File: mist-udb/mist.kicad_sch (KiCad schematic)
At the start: 26 parts, among them J1 78171-0004, J2 Conn_01x05, Q3 MMUN2133LT1G, U3 XC6206PxxxMR-Regulator_Linear, U4 CR2013-MI2120, U5 STM32G474RETx, U6 SN74AHCT1G125DBVR

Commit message: Updated UDB files
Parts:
- added H1, H2, H3, H4, H5, H6: MountingHole_Pad, MountingHole:MountingHole_3.2mm_M3_DIN965_Pad, symbol Mechanical:MountingHole_Pad
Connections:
- net GND: now also H1.1, H2.1, H3.1, H4.1, H5.1, H6.1

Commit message: Updated standoff sizes
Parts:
- H1, H2, H3, H4, H5, H6: footprint MountingHole:MountingHole_3.2mm_M3_DIN965_Pad -> MountingHole:MountingHole_2.2mm_M2_DIN965_Pad
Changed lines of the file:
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@@
 			)
 		)
-		(property "Footprint" "MountingHole:MountingHole_3.2mm_M3_DIN965_Pad"
+		(property "Footprint" "MountingHole:MountingHole_2.2mm_M2_DIN965_Pad"
 			(at 342.9 135.89 0)
 			(effects
@@
 			)
 		)
-		(property "Footprint" "MountingHole:MountingHole_3.2mm_M3_DIN965_Pad"
+		(property "Footprint" "MountingHole:MountingHole_2.2mm_M2_DIN965_Pad"
 			(at 340.36 111.76 0)
 			(effects
@@
 			)
 		)
-		(property "Footprint" "MountingHole:MountingHole_3.2mm_M3_DIN965_Pad"
+		(property "Footprint" "MountingHole:MountingHole_2.2mm_M2_DIN965_Pad"
 			(at 340.36 121.92 0)
 			(effects
@@
 			)
 		)
-		(property "Footprint" "MountingHole:MountingHole_3.2mm_M3_DIN965_Pad"
+		(property "Footprint" "MountingHole:MountingHole_2.2mm_M2_DIN965_Pad"
 			(at 340.36 132.08 0)
 			(effects
@@
 			)
 		)
-		(property "Footprint" "MountingHole:MountingHole_3.2mm_M3_DIN965_Pad"
+		(property "Footprint" "MountingHole:MountingHole_2.2mm_M2_DIN965_Pad"
 			(at 342.9 115.57 0)
 			(effects
@@
 			)
 		)
-		(property "Footprint" "MountingHole:MountingHole_3.2mm_M3_DIN965_Pad"
+		(property "Footprint" "MountingHole:MountingHole_2.2mm_M2_DIN965_Pad"
 			(at 342.9 125.73 0)
 			(effects

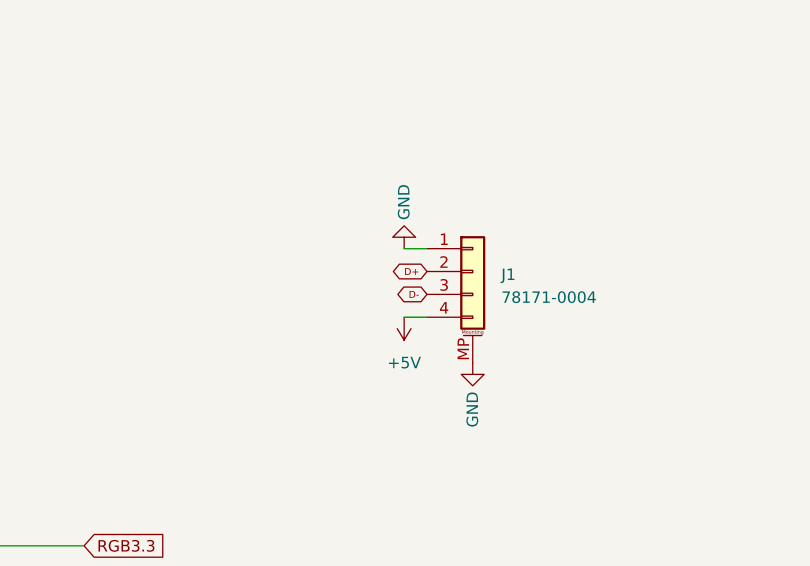
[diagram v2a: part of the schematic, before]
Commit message: Fixed UDB pinout, had it backwards
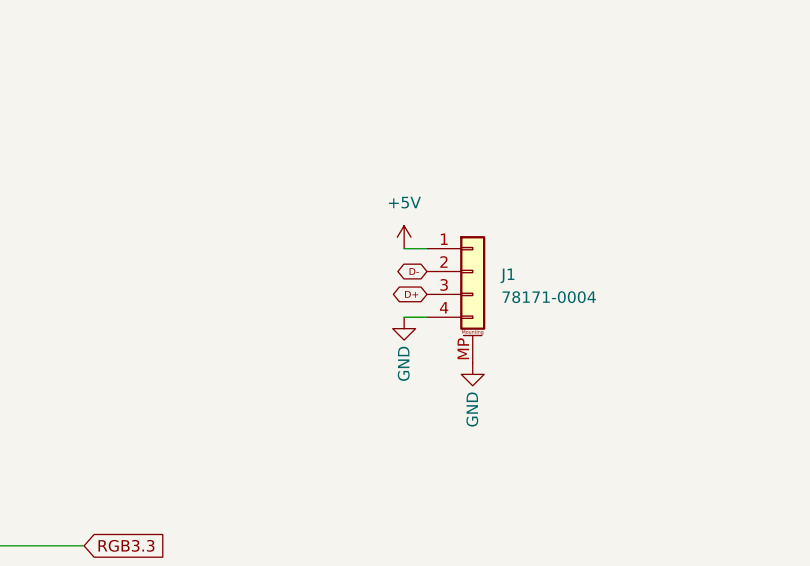
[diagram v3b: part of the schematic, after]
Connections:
- net +5V: now also J1.1 (Pin_1); no longer J1.4 (Pin_4)
- net D+: now also J1.3 (Pin_3); no longer J1.2 (Pin_2)
- net D-: now also J1.2 (Pin_2); no longer J1.3 (Pin_3)
- net GND: now also J1.4 (Pin_4); no longer J1.1 (Pin_1)
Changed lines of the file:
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@@
 	(wire
 		(pts
-			(xy 138.43 45.72) (xy 140.97 45.72)
+			(xy 138.43 38.1) (xy 140.97 38.1)
 		)
 		(stroke
@@
 	(wire
 		(pts
-			(xy 138.43 38.1) (xy 140.97 38.1)
+			(xy 138.43 45.72) (xy 140.97 45.72)
 		)
 		(stroke
@@
 	(global_label "D-"
 		(shape bidirectional)
-		(at 140.97 43.18 180)
+		(at 140.97 40.64 180)
 		(fields_autoplaced yes)
 		(effects
@@
 		)
 		(property "Intersheetrefs" "${INTERSHEET_REFS}"
-			(at 137.8167 43.1324 0)
+			(at 137.8167 40.6876 0)
 			(effects
 				(font
@@
 	(global_label "D+"
 		(shape bidirectional)
-		(at 140.97 40.64 180)
+		(at 140.97 43.18 180)
 		(fields_autoplaced yes)
 		(effects
@@
 		)
 		(property "Intersheetrefs" "${INTERSHEET_REFS}"
-			(at 137.8167 40.5924 0)
+			(at 137.8167 43.2276 0)
 			(effects
 				(font
@@
 	(symbol
 		(lib_id "power:+5V")
-		(at 138.43 45.72 0)
-		(mirror x)
+		(at 138.43 38.1 0)
 		(unit 1)
 		(exclude_from_sim no)
@@
 		)
 		(property "Value" "+5V"
-			(at 138.43 50.8 0)
+			(at 138.43 33.02 0)
 			(effects
 				(font
@@
 		)
 		(property "Footprint" ""
-			(at 138.43 45.72 0)
+			(at 138.43 38.1 0)
 			(effects
 				(font
@@
 		)
 		(property "Datasheet" ""
-			(at 138.43 45.72 0)
+			(at 138.43 38.1 0)
 			(effects
 				(font
@@
 		)
 		(property "Description" ""
-			(at 138.43 45.72 0)
+			(at 138.43 38.1 0)
 			(effects
 				(font
@@
 	(symbol
 		(lib_id "power:GND")
-		(at 138.43 38.1 0)
-		(mirror x)
+		(at 138.43 45.72 0)
 		(unit 1)
 		(exclude_from_sim no)
@@
 		(dnp no)
 		(property "Reference" "#PWR02"
-			(at 138.43 31.75 0)
+			(at 138.43 52.07 0)
 			(effects
 				(font
@@
 		)
 		(property "Value" "GND"
-			(at 138.43 34.925 90)
+			(at 138.43 48.895 90)
 			(effects
 				(font
@@
 		)
 		(property "Footprint" ""
-			(at 138.43 38.1 0)
+			(at 138.43 45.72 0)
 			(effects
 				(font
@@
 		)
 		(property "Datasheet" ""
-			(at 138.43 38.1 0)
+			(at 138.43 45.72 0)
 			(effects
 				(font
@@
 		)
 		(property "Description" ""
-			(at 138.43 38.1 0)
+			(at 138.43 45.72 0)
 			(effects
 				(font
